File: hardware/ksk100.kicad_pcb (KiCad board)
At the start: 2 copper layers, 48 parts, among them J1 USB_OTG, J2 Conn_01x02, J3 Conn_02x06_Odd_Even, J4 Conn_02x06_Odd_Even, J5 Conn_02x05_Odd_Even, SW1 BOOT, SW2 RESET, U1 LT1117-3.3, U2 BQ21040, U3 ESP-12F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

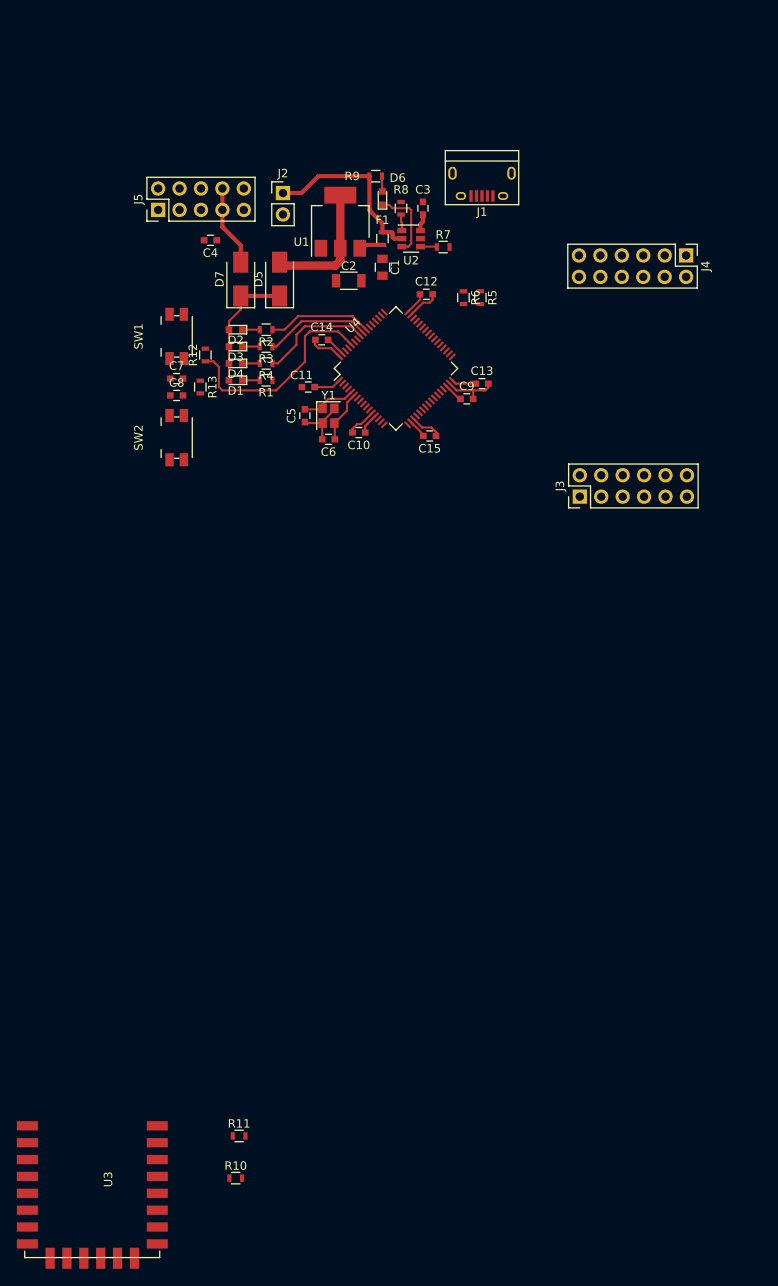
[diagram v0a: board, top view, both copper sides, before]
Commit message: Finish work on the v1.0 PCB
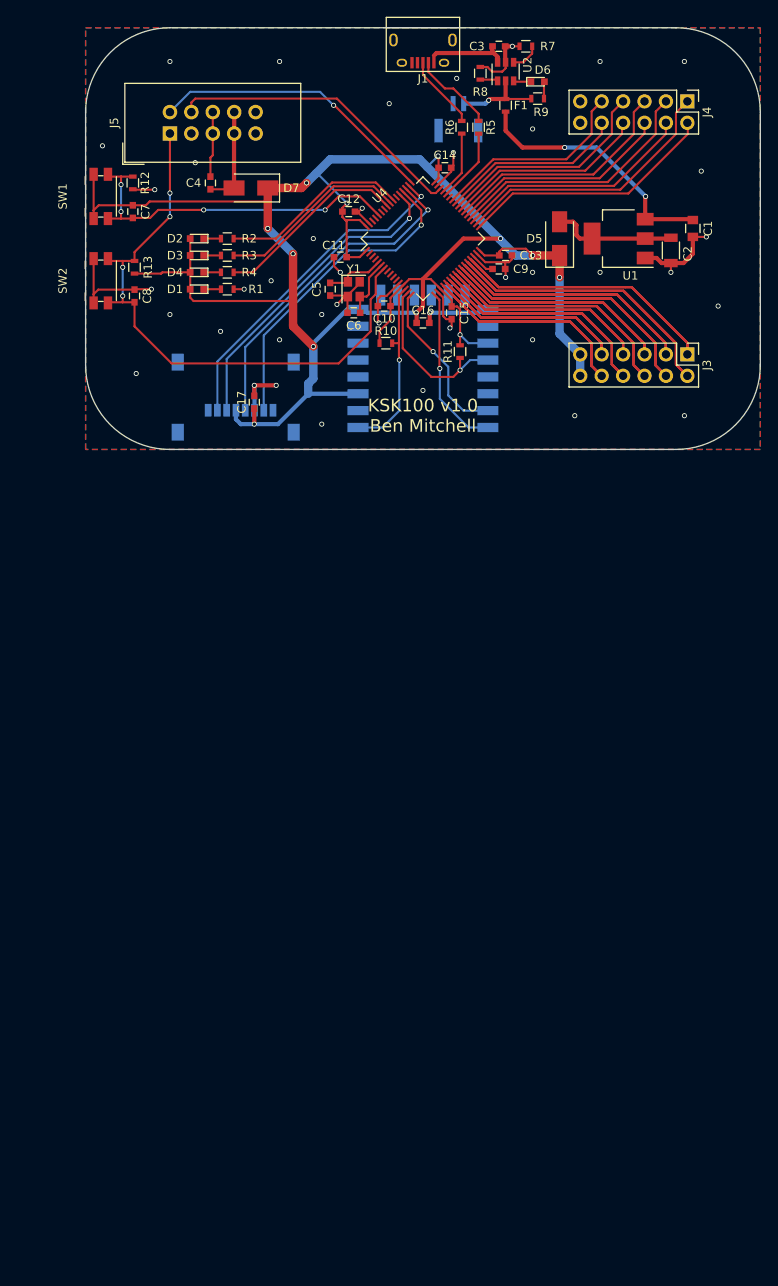
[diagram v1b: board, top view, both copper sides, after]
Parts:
- added C16: 100nF, Capacitors_SMD:C_0603, F.Cu at (90.0, 85.0)
- added C17: 100nF, Capacitors_SMD:C_0603, F.Cu at (70.0, 94.4)
- added J6: Micro_SD_Card, Connectors_Card:MicroSd_Wurth_693072010801, B.Cu at (67.8, 93.8)
- C4: value 1uF -> 10uF
- J2: footprint Pin_Headers:Pin_Header_Straight_1x02_Pitch2.54mm -> Connectors_JST:JST_GH_SM02B-GHS-TB_02x1.25mm_Angled; moved to B.Cu
- J5: footprint Pin_Headers:Pin_Header_Straight_2x05_Pitch2.54mm -> Connectors_IDC:IDC-Header_2x05_Pitch2.54mm_Straight
- U3: moved to B.Cu
- moved R10 100.6 mm to (85.6, 87.4)
- moved R11 96.6 mm to (94.4, 88.4), turned to 90 degrees
- moved U3 91.6 mm to (83.0, 97.4)
- moved C2 38.4 mm to (119.4, 76.4), turned to 270 degrees
- moved C1 37.1 mm to (122.0, 73.8)
- moved D5 33.5 mm to (106.2, 75.0)
- moved U1 33.1 mm to (113.2, 75.0), turned to 180 degrees
- moved R7 25.7 mm to (102.2, 52.2), turned to 180 degrees
- moved C14 25.1 mm to (92.6, 66.6)
- moved D6 23.0 mm to (103.6, 56.4), turned to 0 degrees
- moved U2 22.7 mm to (99.8, 55.2), turned to 90 degrees
- moved J2 22.7 mm to (94.2, 60.6), turned to 180 degrees
- moved R12 22.1 mm to (55.6, 68.4), turned to 270 degrees
- moved F1 21.5 mm to (99.8, 59.2)
- moved R9 21.3 mm to (103.6, 58.4)
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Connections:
- J3 pad 1: /PA4 -> /PB10
- J3 pad 10: /PB10 -> /PA4
- J3 pad 11: GND -> +3V3
- J3 pad 12: GND -> +3V3
- J3 pad 2: /PA5 -> /PB2
- J3 pad 3: /PA6 -> /PB1
- J3 pad 4: /PA7 -> /PB0
- J3 pad 5: /PC4 -> /PC5
- J3 pad 6: /PC5 -> /PC4
- J3 pad 7: /PB0 -> /PA7
- J3 pad 8: /PB1 -> /PA6
- J3 pad 9: /PB2 -> /PA5
- J4 pad 1: /PB12 -> /PB13
- J4 pad 10: /PA9 -> /PA8
- J4 pad 11: +3V3 -> GND
- J4 pad 12: +3V3 -> GND
- J4 pad 2: /PB13 -> /PB12
- J4 pad 3: /PB14 -> /PB15
- J4 pad 4: /PB15 -> /PB14
- J4 pad 5: /PC6 -> /PC7
- J4 pad 6: /PC7 -> /PC6
- J4 pad 7: /PC8 -> /PC9
- J4 pad 8: /PC9 -> /PC8
- J4 pad 9: /PA8 -> /PA9
- U4 pad 50: (no net) -> /PA15
- U4 pad 51: (no net) -> /PC10
- U4 pad 52: (no net) -> /PC11
- U4 pad 53: (no net) -> /PC12
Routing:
- net +3V3: track 34.6 -> 242.3 mm, vias 0 -> 12
- net /PB2: track 0.00 -> 132.6 mm
- net /PB10: track 0.00 -> 125.0 mm
- net /PB0: track 0.00 -> 124.4 mm
- net /PB1: track 0.00 -> 116.2 mm
- net /PC4: track 0.00 -> 115.7 mm
- net /PC5: track 0.00 -> 107.6 mm
- net /PA6: track 0.00 -> 107.1 mm
- net /PA7: track 0.00 -> 99.4 mm
- net /PA4: track 0.00 -> 98.9 mm
- net /PA5: track 0.00 -> 90.7 mm
- net /nRESET: track 0.00 -> 70.6 mm, vias 0 -> 4
- net GND: track 25.3 -> 95.0 mm, vias 0 -> 41
- net /PA15: track 0.00 -> 40.1 mm, vias 0 -> 1
- net /PC10: track 0.00 -> 39.6 mm, vias 0 -> 1
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- added copper zone on B.Cu, net GND
- added copper zone on F.Cu, net GND
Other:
- board outline added: 80 x 50 mm
- board text added: "KSK100 v1.0 Ben Mitchell"

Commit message: Plot the gerbers and start working on the motor driver
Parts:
- added REF**: VIA, VIA, F.Cu at (74.0, 93.4)
- added REF**: VIA, VIA, F.Cu at (111.0, 79.0)
- added REF**: VIA, VIA, F.Cu at (108.0, 96.0)
- added REF**: VIA, VIA, F.Cu at (103.0, 87.0)
- added REF**: VIA, VIA, F.Cu at (90.0, 93.0)
- added REF**: VIA, VIA, F.Cu at (56.0, 91.0)
- added REF**: VIA, VIA, F.Cu at (78.0, 97.0)
- added REF**: VIA, VIA, F.Cu at (78.0, 84.0)
- added REF**: VIA, VIA, F.Cu at (73.0, 87.0)
- added REF**: VIA, VIA, F.Cu at (60.0, 84.0)
- added REF**: VIA, VIA, F.Cu at (66.0, 86.0)
- added REF**: VIA, VIA, F.Cu at (98.6, 64.0)
- added REF**: VIA, VIA, F.Cu at (72.0, 80.0)
- added REF**: VIA, VIA, F.Cu at (77.0, 75.0)
- added REF**: VIA, VIA, F.Cu at (86.0, 59.0)
- added REF**: VIA, VIA, F.Cu at (73.0, 54.0)
- added REF**: VIA, VIA, F.Cu at (60.0, 54.0)
- added REF**: VIA, VIA, F.Cu at (52.0, 64.0)
- added REF**: VIA, VIA, F.Cu at (123.0, 55.0)
- added REF**: VIA, VIA, F.Cu at (125.0, 67.0)
- added REF**: VIA, VIA, F.Cu at (111.0, 54.0)
- added REF**: VIA, VIA, F.Cu at (103.0, 62.0)
- added REF**: VIA, VIA, F.Cu at (125.0, 83.0)
- added REF**: VIA, VIA, F.Cu at (121.0, 96.0)
- added REF**: VIA, VIA, F.Cu at (103.0, 79.0)
- moved J5 3.55 mm to (63.2, 61.0)
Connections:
- C7 pad 2: /MCU/BOOT -> /BOOT
- R12 pad 1: /MCU/BOOT -> /BOOT
- SW1 pad 2: /MCU/BOOT -> /BOOT
- U4 pad 43: (no net) -> /BOOT
- U4 pad 60: /MCU/BOOT -> /BOOT
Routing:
- net /BOOT: track 0.00 -> 54.3 mm, vias 0 -> 4
- net /MCU/BOOT: track 42.1 -> 0.00 mm, vias 4 -> 0
- net GND: track 95.0 -> 87.5 mm, vias 41 -> 18
- net /nRESET: track 70.6 -> 74.5 mm
- net Net-(C4-Pad1): track 11.9 -> 14.7 mm
- net /PA13: track 35.8 -> 33.2 mm
- net /PA14: track 34.1 -> 32.2 mm
- net (no net): track 0.00 -> 1.20 mm, vias 0 -> 1
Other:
- board text added: "RESET"
